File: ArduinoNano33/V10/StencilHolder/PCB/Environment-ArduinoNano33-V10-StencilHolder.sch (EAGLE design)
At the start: 10 parts

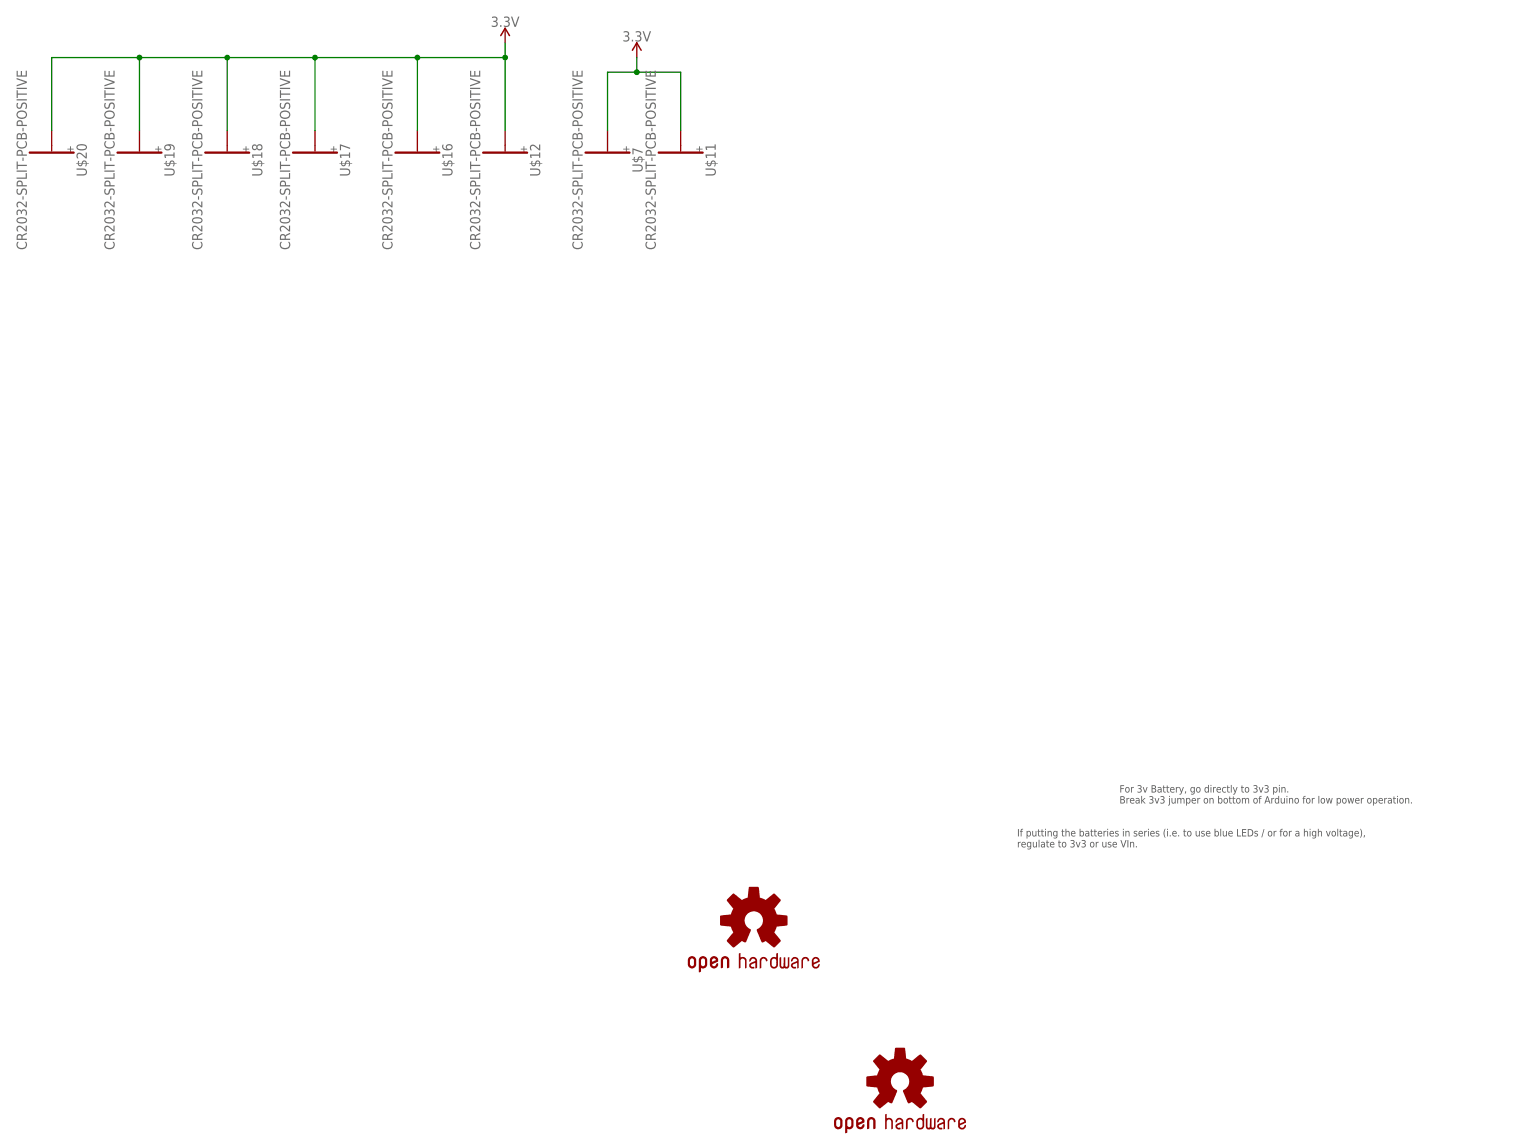
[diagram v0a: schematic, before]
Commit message: Update for V10.1 with improvements...
* Removed USB C until I get a better foot print for the ones I can buy and replaced with Micro B
* Reduced cutout in middle layers as it doesn't need so much space.
* Increased hole size in middle layers for potential NFC wire passthrough to prevent clashes with solder
* Added potential extra solder connection for bottom to middle layers.
* Changed bottom boards so they use a top side pad to be soldered to rather than a hole to make the bottom face tidier.
* Removed switch on the top board as it would have been weird to use
* Added potential divider for the "3v3" supply to allow monitoring of battery voltage (although this may drain the battery too much)
* Extended the pads (where possible) for the Arduino to make hand soldering it to the board easier.
* Improved top level silk screen text
* Added "Up" to the bottom/middle layers to aid assembly.
* Fixed issue with missing holes on the non-key chain middle layer.
* Improved custom bottoms to be one PCB per customisation
* General tidy up of the reference lines
* Improved (fixed!) some of the filenames

Sent to JLCPCB - 27 Feb 2020
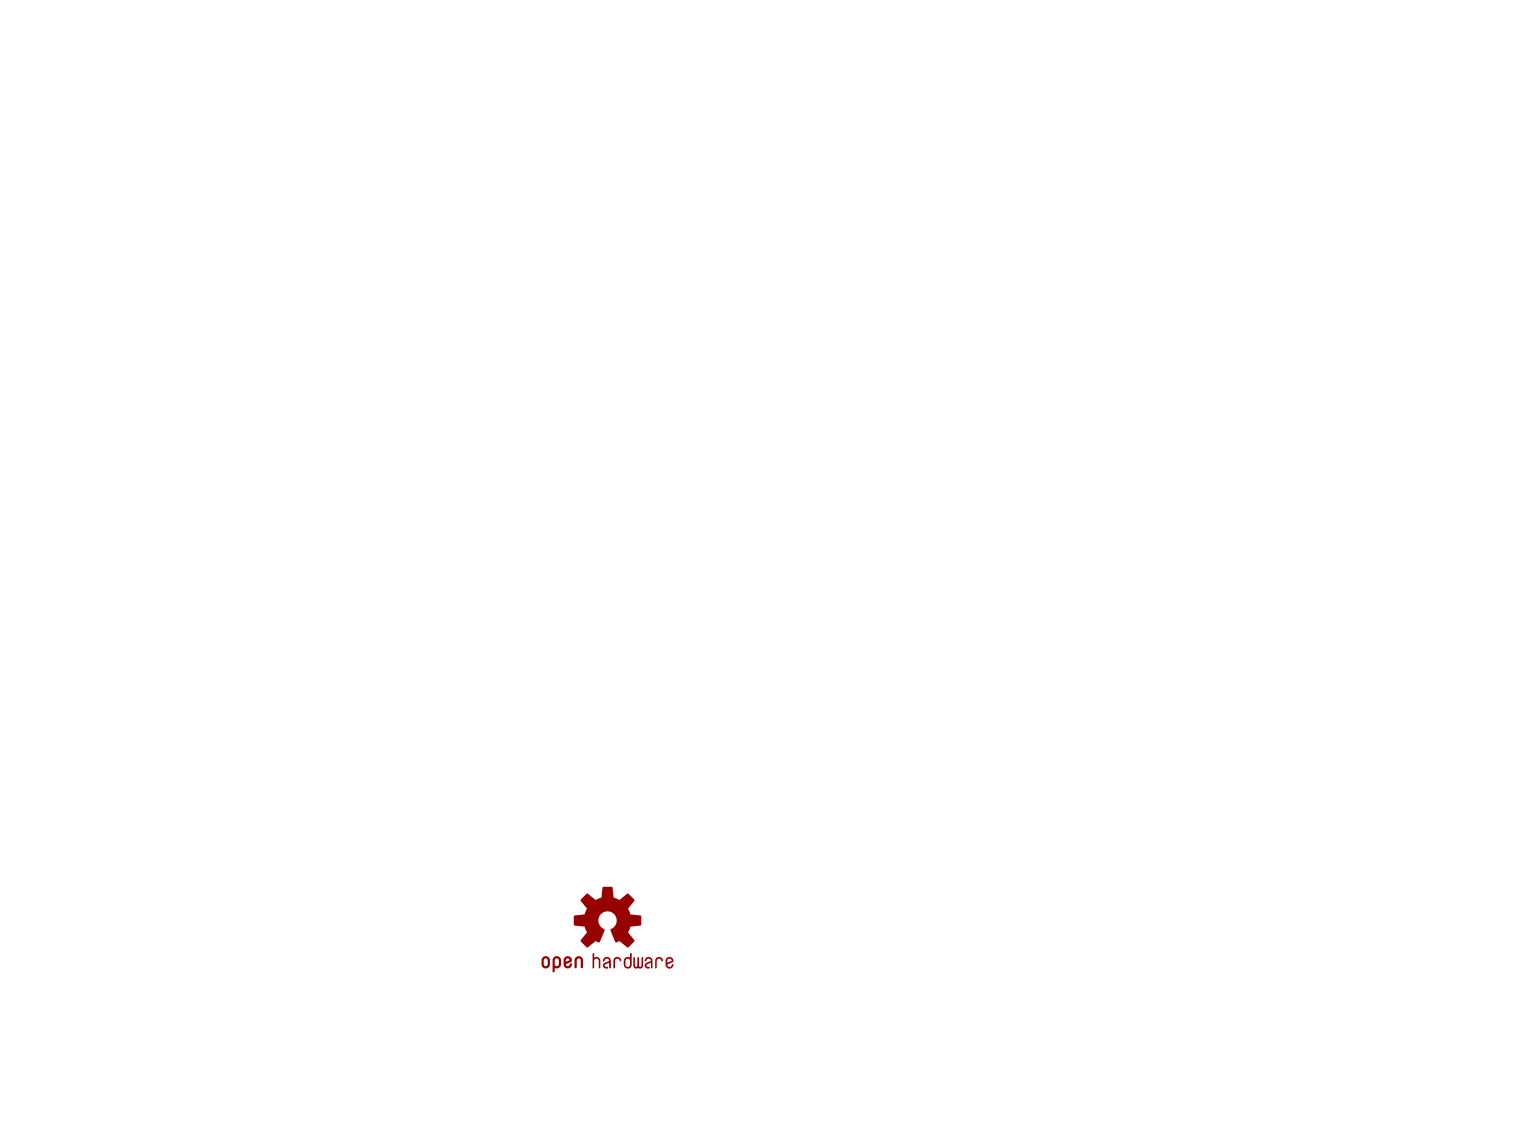
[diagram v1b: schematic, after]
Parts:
- removed LOGO2: OSHW-LOGOL, SparkFun-Aesthetics:OSHW-LOGOL
- removed LOGO7: OSHW-LOGOM, SparkFun-Aesthetics:OSHW-LOGOM
- removed U$11, U$12, U$16, U$17, U$18, U$19, U$20, U$7: CR2032-SPLIT-PCB-POSITIVE, ThingySticks:CR2032-SPLIT-PCB-POSITIVE
- added LOGO3: OSHW-LOGOL, SparkFun-Aesthetics:OSHW-LOGOL
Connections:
- removed net 3.3V: U$11.+, U$12.+, U$16.+, U$17.+, U$18.+, U$19.+, U$20.+, U$7.+
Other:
- note removed: "For 3v Battery, go directly to 3v3 pin. Break 3v3 jumper on bottom of Arduino for low power operation."
- note removed: "If putting the batteries in series (i.e. to use blue LEDs / or for a high voltage), regulate to 3v3 or use VIn."
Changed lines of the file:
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@@
 <parts>
 <part name="FRAME1" library="SparkFun-Aesthetics" deviceset="FRAME-A4L" device=""/>
-<part name="LOGO2" library="SparkFun-Aesthetics" deviceset="OSHW-LOGO" device="L"/>
-<part name="U$7" library="ThingySticks" deviceset="CR2032-SPLIT-PCB-POSITIVE" device=""/>
-<part name="U$11" library="ThingySticks" deviceset="CR2032-SPLIT-PCB-POSITIVE" device=""/>
-<part name="SUPPLY2" library="SparkFun-PowerSymbols" deviceset="3.3V" device=""/>
-<part name="LOGO7" library="SparkFun-Aesthetics" deviceset="OSHW-LOGO" device="M"/>
-<part name="U$12" library="ThingySticks" deviceset="CR2032-SPLIT-PCB-POSITIVE" device=""/>
-<part name="U$16" library="ThingySticks" deviceset="CR2032-SPLIT-PCB-POSITIVE" device=""/>
-<part name="U$17" library="ThingySticks" deviceset="CR2032-SPLIT-PCB-POSITIVE" device=""/>
-<part name="U$18" library="ThingySticks" deviceset="CR2032-SPLIT-PCB-POSITIVE" device=""/>
-<part name="U$19" library="ThingySticks" deviceset="CR2032-SPLIT-PCB-POSITIVE" device=""/>
-<part name="U$20" library="ThingySticks" deviceset="CR2032-SPLIT-PCB-POSITIVE" device=""/>
-<part name="SUPPLY14" library="SparkFun-PowerSymbols" deviceset="3.3V" device=""/>
+<part name="LOGO3" library="SparkFun-Aesthetics" deviceset="OSHW-LOGO" device="L"/>
 </parts>
 <sheets>
 <sheet>
 <plain>
-<text x="104.14" y="15.24" size="1.27" layer="97">For 3v Battery, go directly to 3v3 pin.
-Break 3v3 jumper on bottom of Arduino for low power operation.</text>
-<text x="86.36" y="7.62" size="1.27" layer="97">If putting the batteries in series (i.e. to use blue LEDs / or for a high voltage),
-regulate to 3v3 or use VIn.</text>
 </plain>
 <instances>
 <instance part="FRAME1" gate="G$1" x="-96.52" y="-17.78"/>
-<instance part="LOGO2" gate="G$1" x="40.64" y="-5.08"/>
-<instance part="U$7" gate="G$1" x="15.24" y="127" rot="R270"/>
-<instance part="U$11" gate="G$1" x="27.94" y="127" rot="R270"/>
-<instance part="SUPPLY2" gate="G$1" x="20.32" y="144.78"/>
-<instance part="LOGO7" gate="G$1" x="66.04" y="-33.02"/>
-<instance part="U$12" gate="G$1" x="-2.54" y="127" rot="R270"/>
-<instance part="U$16" gate="G$1" x="-17.78" y="127" rot="R270"/>
-<instance part="U$17" gate="G$1" x="-35.56" y="127" rot="R270"/>
-<instance part="U$18" gate="G$1" x="-50.8" y="127" rot="R270"/>
-<instance part="U$19" gate="G$1" x="-66.04" y="127" rot="R270"/>
-<instance part="U$20" gate="G$1" x="-81.28" y="127" rot="R270"/>
-<instance part="SUPPLY14" gate="G$1" x="-2.54" y="147.32"/>
+<instance part="LOGO3" gate="G$1" x="15.24" y="-5.08"/>
 </instances>
 <busses>
 </busses>
 <nets>
-<net name="3.3V" class="0">
-<segment>
-<pinref part="U$7" gate="G$1" pin="+"/>
-<wire x1="15.24" y1="132.08" x2="15.24" y2="142.24" width="0.1524" layer="91"/>
-<pinref part="U$11" gate="G$1" pin="+"/>
-<wire x1="15.24" y1="142.24" x2="20.32" y2="142.24" width="0.1524" layer="91"/>
-<wire x1="20.32" y1="142.24" x2="27.94" y2="142.24" width="0.1524" layer="91"/>
-<wire x1="27.94" y1="142.24" x2="27.94" y2="132.08" width="0.1524" layer="91"/>
-<wire x1="20.32" y1="142.24" x2="20.32" y2="144.78" width="0.1524" layer="91"/>
-<pinref part="SUPPLY2" gate="G$1" pin="3.3V"/>
-<junction x="20.32" y="142.24"/>
-</segment>
-<segment>
-<pinref part="U$20" gate="G$1" pin="+"/>
-<wire x1="-81.28" y1="132.08" x2="-81.28" y2="144.78" width="0.1524" layer="91"/>
-<pinref part="U$12" gate="G$1" pin="+"/>
-<wire x1="-81.28" y1="144.78" x2="-66.04" y2="144.78" width="0.1524" layer="91"/>
-<wire x1="-66.04" y1="144.78" x2="-50.8" y2="144.78" width="0.1524" layer="91"/>
-<wire x1="-50.8" y1="144.78" x2="-35.56" y2="144.78" width="0.1524" layer="91"/>
-<wire x1="-35.56" y1="144.78" x2="-17.78" y2="144.78" width="0.1524" layer="91"/>
-<wire x1="-17.78" y1="144.78" x2="-2.54" y2="144.78" width="0.1524" layer="91"/>
-<wire x1="-2.54" y1="144.78" x2="-2.54" y2="132.08" width="0.1524" layer="91"/>
-<wire x1="-2.54" y1="144.78" x2="-2.54" y2="147.32" width="0.1524" layer="91"/>
-<pinref part="SUPPLY14" gate="G$1" pin="3.3V"/>
-<junction x="-2.54" y="144.78"/>
-<pinref part="U$19" gate="G$1" pin="+"/>
-<wire x1="-66.04" y1="132.08" x2="-66.04" y2="144.78" width="0.1524" layer="91"/>
-<pinref part="U$18" gate="G$1" pin="+"/>
-<wire x1="-50.8" y1="132.08" x2="-50.8" y2="144.78" width="0.1524" layer="91"/>
-<pinref part="U$17" gate="G$1" pin="+"/>
-<wire x1="-35.56" y1="132.08" x2="-35.56" y2="144.78" width="0.1524" layer="91"/>
-<pinref part="U$16" gate="G$1" pin="+"/>
-<wire x1="-17.78" y1="132.08" x2="-17.78" y2="144.78" width="0.1524" layer="91"/>
-<junction x="-66.04" y="144.78"/>
-<junction x="-50.8" y="144.78"/>
-<junction x="-35.56" y="144.78"/>
-<junction x="-17.78" y="144.78"/>
-</segment>
-</net>
 </nets>
 </sheet>
@@
 </schematic>
 </drawing>
-<compatibility>
-<note version="6.3" minversion="6.2.2" severity="warning">
-Since Version 6.2.2 text objects can contain more than one line,
-which will not be processed correctly with this version.
-</note>
-</compatibility>
 </eagle>
